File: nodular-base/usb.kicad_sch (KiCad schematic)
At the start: 7 parts, among them J7 USB_C_Receptacle_USB2.0, J8 USB_C_Receptacle_USB2.0, U2 FUSB302BMPX, U3 BQ25895RTW

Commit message: WIP layout for base
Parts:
- added C13 (x6): 10uF, Capacitor_SMD:C_1206_3216Metric, symbol Device:C
- added C25: 4.7uF, Capacitor_SMD:C_0603_1608Metric, symbol Device:C
- added C26, C31: 47nF, Capacitor_SMD:C_0402_1005Metric, symbol Device:C
- added C30: 1uF, Capacitor_SMD:C_0603_1608Metric, symbol Device:C
- added J10: Conn_01x02, JST_PH_B2B-PH-SM4-TB_1x02-1MP_P2.00mm_Vertical, symbol Connector_Generic:Conn_01x02
- added L2: L, Inductor_SMD_Wurth:L_Wurth_WE-LQSH-4020, symbol Device:L
- added L3: L, Inductor_SMD_Wurth:L_Wurth_WE-LQSH-2512, symbol Device:L
- added R27: 2k2, Resistor_SMD:R_0402_1005Metric, symbol Device:R
- added R28, R32: R, Resistor_SMD:R_0402_1005Metric, symbol Device:R
- added R29, R30, R31: 10k, Resistor_SMD:R_0402_1005Metric, symbol Device:R
- added U29: RCLAMP0524P-ES, Package_DFN_QFN:Diodes_UDFN-10_1.0x2.5mm_P0.5mm, symbol nodular:RCLAMP0524P-ES
- added U43: TLV62595DMQR, nodular:Texas_VSON-HR-6_1.5x1.5mm_P0.5mm, symbol nodular:TLV62595DMQR
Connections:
- net GND: now also J8.A1 (GND), J8.A12 (GND), J8.B1 (GND), J8.B12 (GND), J8.S1 (SHIELD), U2.15 (GND), U2.8 (GND), U2.9 (GND), U3.17 (PGND), U3.18 (PGND), U3.25 (PGND), U3.9 (~{CE}), C13.2, C13.2, C13.2, C13.2, C13.2, C13.2, C25.2, C30.2, J10.2 (Pin_2), R29.2, R31.1, R32.1, U29.3 (GND), U29.8 (GND), U43.4 (GND)
- net USB+: now also U29.5 (CHD), U29.6 (CHD)
- net USB-: now also U29.4 (CHC), U29.7 (CHC)
- net STAT: now reaches D1.1 (K)
- net STAT: now also U3.4 (STAT)
- net at D1.2 (A): now also R27.1
- net VBUS: now reaches J7.A4 (VBUS), J7.A9 (VBUS), J7.B4 (VBUS), J7.B9 (VBUS), U2.2 (VBUS)
- net VBUS: now also U3.1 (VBUS), C30.1
- net CC1: now reaches J7.A5 (CC1), R1.1, U2.10 (CC1), U2.11 (CC1)
- net CC1: now also U29.2 (CHB), U29.9 (CHB)
- net CC2: now reaches J7.B5 (CC2), R2.1, U2.1 (CC2), U2.14 (CC2)
- net CC2: now also U29.1 (CHA), U29.10 (CHA)
- net at J8.A6 (D+): now also J8.B6 (D+)
- net at J8.A7 (D-): now also J8.B7 (D-)
- net 3V3_SYS: now reaches U2.3 (VDD), U2.4 (VDD)
- net 3V3_SYS: now also C13.1, C13.1, C13.1, C31.1, L3.2, R27.2, R28.2
- net SCL: now reaches U2.6 (SCL)
- net SCL: now also U3.5 (SCL)
- net SDA: now reaches U2.7 (SDA)
- net SDA: now also U3.6 (SDA)
- net at U3.10 (ILIM): now also R29.1
- net at U3.11 (TS): now also R30.1, R31.2
- net ~{QON}: now reaches U3.12 (~{QON})
- net BAT+: now reaches U3.13 (BAT), U3.14 (BAT)
- net BAT+: now also C13.1, J10.1 (Pin_1)
- net VSYS: now reaches U3.15 (SYS), U3.16 (SYS)
- net VSYS: now also C13.1, C13.1, L2.2, U43.1 (EN), U43.6 (VIN)
- net at U3.19 (SW), U3.20 (SW): now also C26.1, L2.1
- net at U3.21 (BTST): now also C26.2
- net at U3.22 (REGN): now also C25.1, R30.2
- new net: C31.2, R28.1, R32.2, U43.3 (FB)
- new net: L3.1, U43.5 (SW)
- no-connect marks 2 -> 8
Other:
- moved on the sheet: D1

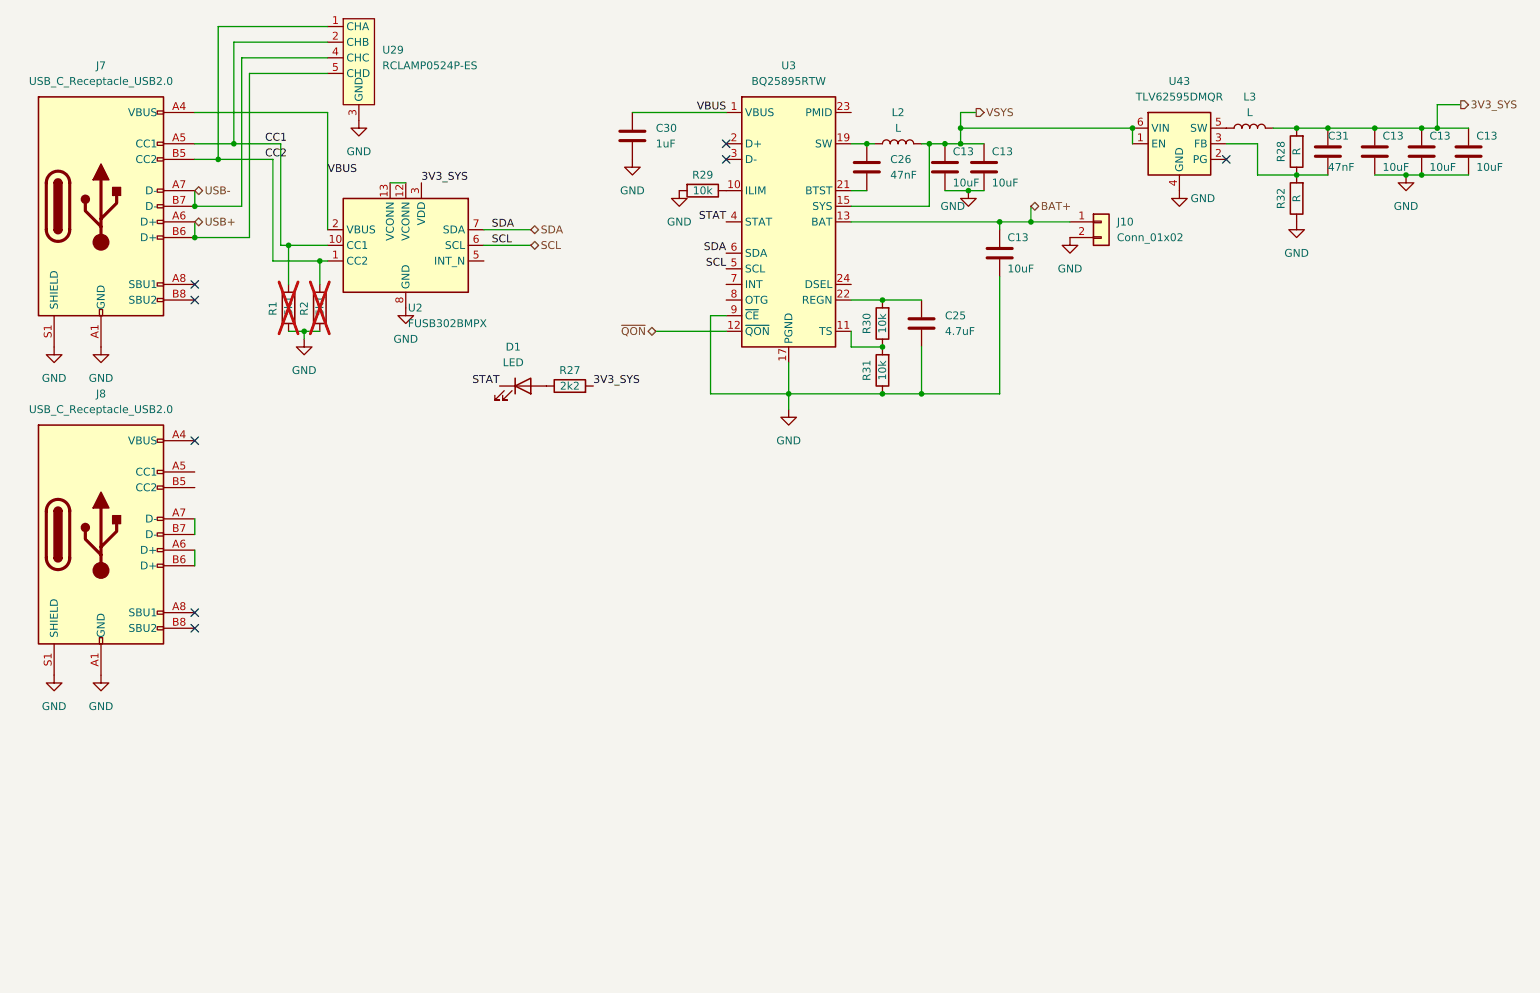
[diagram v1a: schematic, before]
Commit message: Switched from CAN to USB for second USB-C port Added second PD controller and USB mux to allow switching between host and device port Added SOICbite to corner All routing complete Updated pin map, added i2c addresses, soicbit pin mapping, and fpc pinout to document
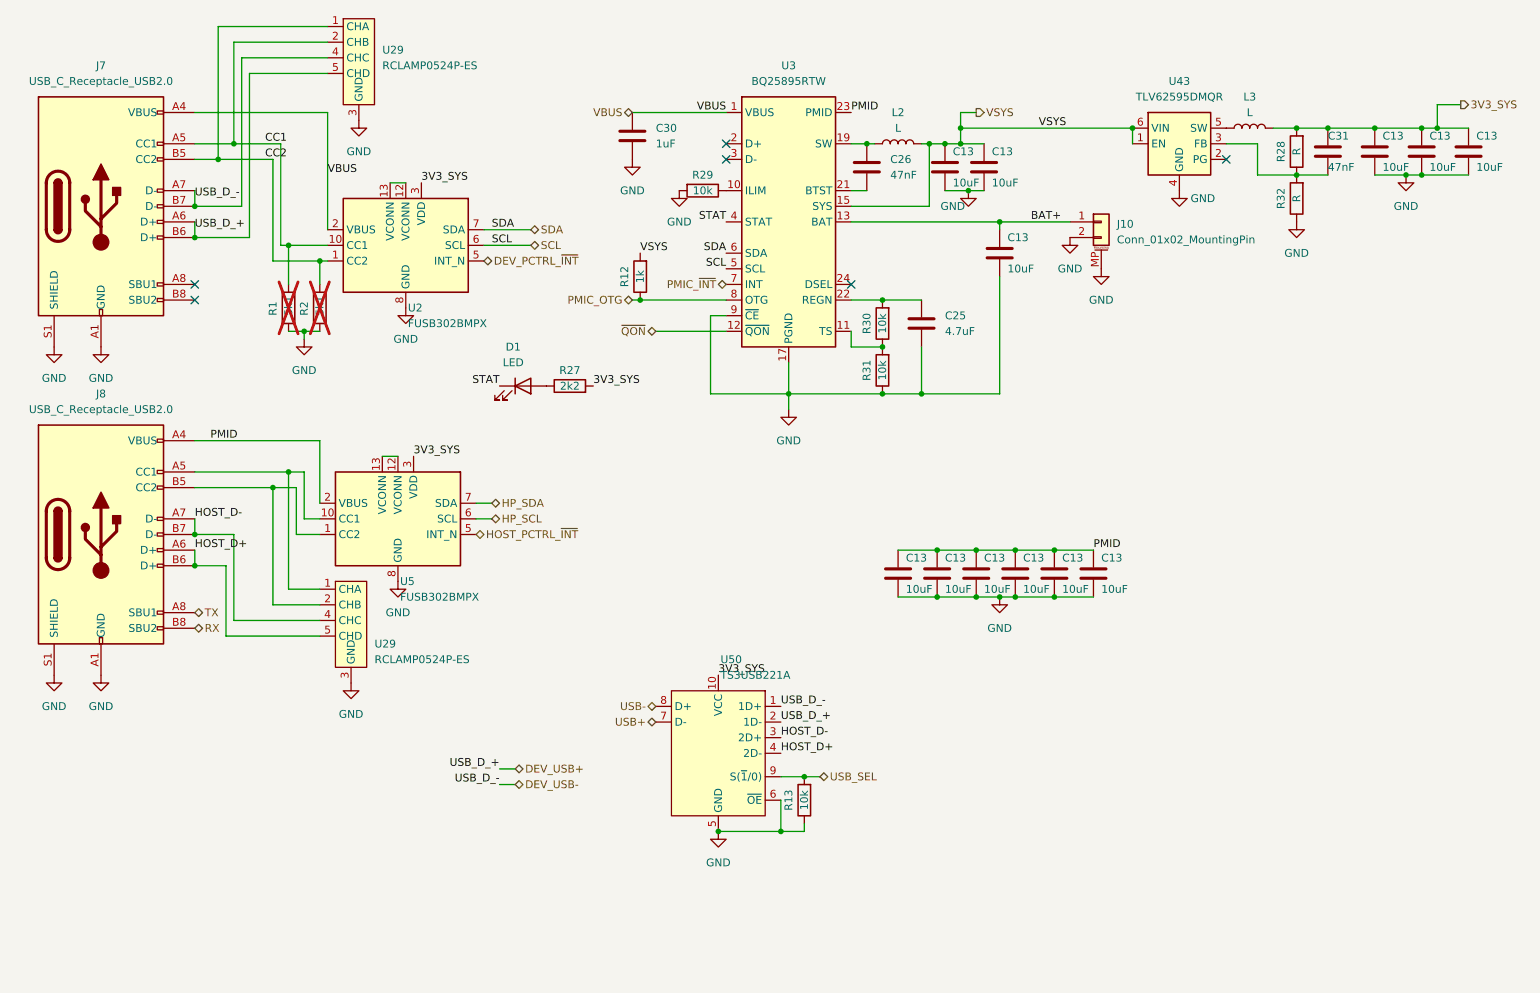
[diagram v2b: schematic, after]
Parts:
- removed J10: Conn_01x02, JST_PH_B2B-PH-SM4-TB_1x02-1MP_P2.00mm_Vertical, symbol Connector_Generic:Conn_01x02
- added C13 (x6): 10uF, Capacitor_SMD:C_1206_3216Metric, symbol Device:C
- added J10: Conn_01x02_MountingPin, JST_PH_B2B-PH-SM4-TB_1x02-1MP_P2.00mm_Vertical, symbol Connector_Generic_MountingPin:Conn_01x02_MountingPin
- added R12: 1k, Resistor_SMD:R_0402_1005Metric, symbol Device:R
- added R13: 10k, Resistor_SMD:R_0402_1005Metric, symbol Device:R
- added U29: RCLAMP0524P-ES, Package_DFN_QFN:Diodes_UDFN-10_1.0x2.5mm_P0.5mm, symbol nodular:RCLAMP0524P-ES
- added U5: FUSB302BMPX, Package_DFN_QFN:WQFN-14-1EP_2.5x2.5mm_P0.5mm_EP1.45x1.45mm, symbol Interface_USB:FUSB302BMPX
- added U50: TS3USB221A, nodular:Texas_PUQFN-10_RSE_1.5x2mm, symbol nodular:TS3USB221A
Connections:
- net 3V3_SYS: now also U5.3 (VDD), U5.4 (VDD), U50.10 (VCC)
- net BAT+: now also J10.1 (Pin_1)
- net GND: now also C13.2, C13.2, C13.2, C13.2, C13.2, C13.2, J10.2 (Pin_2), J10.MP (MountPin), R13.1, U29.3 (GND), U29.8 (GND), U5.15 (GND), U5.8 (GND), U5.9 (GND), U50.5 (GND), U50.6 (~{OE})
- net USB+: now also U50.7 (D-); no longer J7.A6 (D+), J7.B6 (D+), U29.5 (CHD), U29.6 (CHD)
- net USB-: now also U50.8 (D+); no longer J7.A7 (D-), J7.B7 (D-), U29.4 (CHC), U29.7 (CHC)
- net VSYS: now also R12.2
- net PMID: now reaches J8.A4 (VBUS), J8.A9 (VBUS), J8.B4 (VBUS), J8.B9 (VBUS)
- net PMID: now also U3.23 (PMID), C13.1, C13.1, C13.1, C13.1, C13.1, C13.1, U5.2 (VBUS)
- net at J8.A5 (CC1): now also U29.1 (CHA), U29.10 (CHA), U5.10 (CC1), U5.11 (CC1)
- net HOST_D+: now reaches J8.A6 (D+), J8.B6 (D+)
- net HOST_D+: now also U29.5 (CHD), U29.6 (CHD), U50.4 (2D-)
- net HOST_D-: now reaches J8.A7 (D-), J8.B7 (D-)
- net HOST_D-: now also U29.4 (CHC), U29.7 (CHC), U50.3 (2D+)
- net TX: now reaches J8.A8 (SBU1)
- net at J8.B5 (CC2): now also U29.2 (CHB), U29.9 (CHB), U5.1 (CC2), U5.14 (CC2)
- net RX: now reaches J8.B8 (SBU2)
- net DEV_PCTRL_~{INT}: now reaches U2.5 (INT_N)
- net PMIC_~{INT}: now reaches U3.7 (INT)
- net PMIC_OTG: now reaches U3.8 (OTG)
- net PMIC_OTG: now also R12.1
- new net: U5.12 (VCONN), U5.13 (VCONN)
- new net DEV_USB+: J7.A6 (D+), J7.B6 (D+), U29.5 (CHD), U29.6 (CHD), U50.2 (1D-)
- new net DEV_USB-: J7.A7 (D-), J7.B7 (D-), U29.4 (CHC), U29.7 (CHC), U50.1 (1D+)
- new net HOST_PCTRL_~{INT}: U5.5 (INT_N)
- new net HP_SCL: U5.6 (SCL)
- new net HP_SDA: U5.7 (SDA)
- new net USB_SEL: R13.2, U50.9 (S(~{1}/0))
- no-connect marks 8 -> 6
